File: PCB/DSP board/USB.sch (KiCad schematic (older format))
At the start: 24 parts, among them J5 USB_B, U8 USB3300-EZK, Y3 24MHz

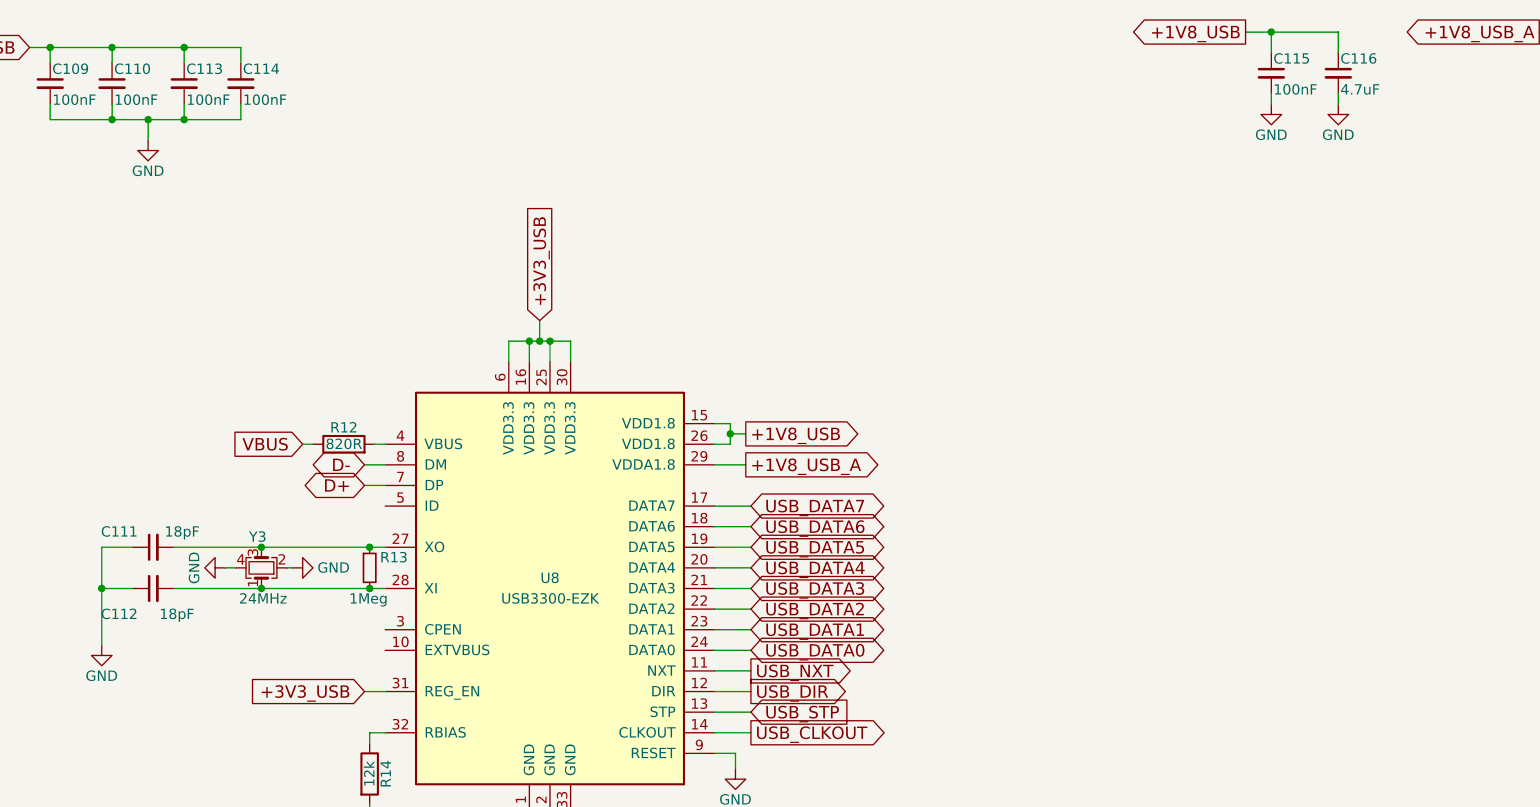
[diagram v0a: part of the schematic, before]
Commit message: Schematics + Footprints Rev.1
Ready to route.
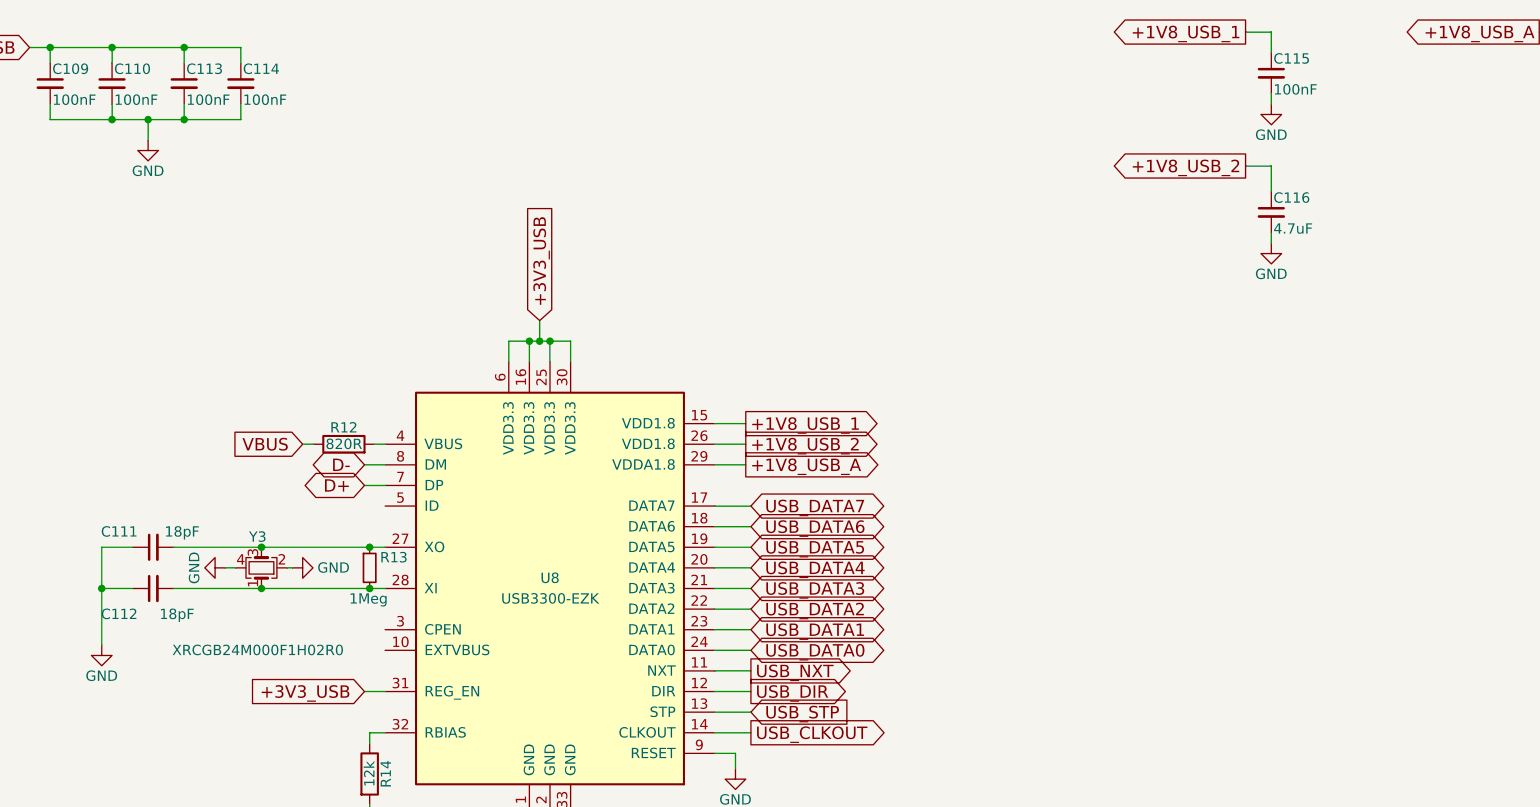
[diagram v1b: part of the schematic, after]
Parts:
- C105, C106, C109, C110, C111, C112, C113, C114, C115, C117: footprint (none) -> Capacitors_SMD:C_0603
- C107, C108, C116, C118: footprint (none) -> Capacitors_SMD:C_0805
- J5: footprint (none) -> USB_Connector:USB_B_2.0
- L12: footprint (none) -> Inductors_SMD:L_0603
- R12, R13, R14: footprint (none) -> Resistors_SMD:R_0603
- RN24, RN25, RN26: footprint (none) -> Resistor:0603_RN4
- Y3: value 24MHz -> XRCGB24M000F1H02R0; footprint (none) -> Crystals:Crystal_SMD_2016-4pin_2.0x1.6mm
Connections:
- net +1V8_USB renamed +1V8_USB_1
- net +1V8_USB_1: no longer C116.1, U8.26 (VDD1.8)
- new net +1V8_USB_2: C116.1, U8.26 (VDD1.8)
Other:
- moved on the sheet: C116

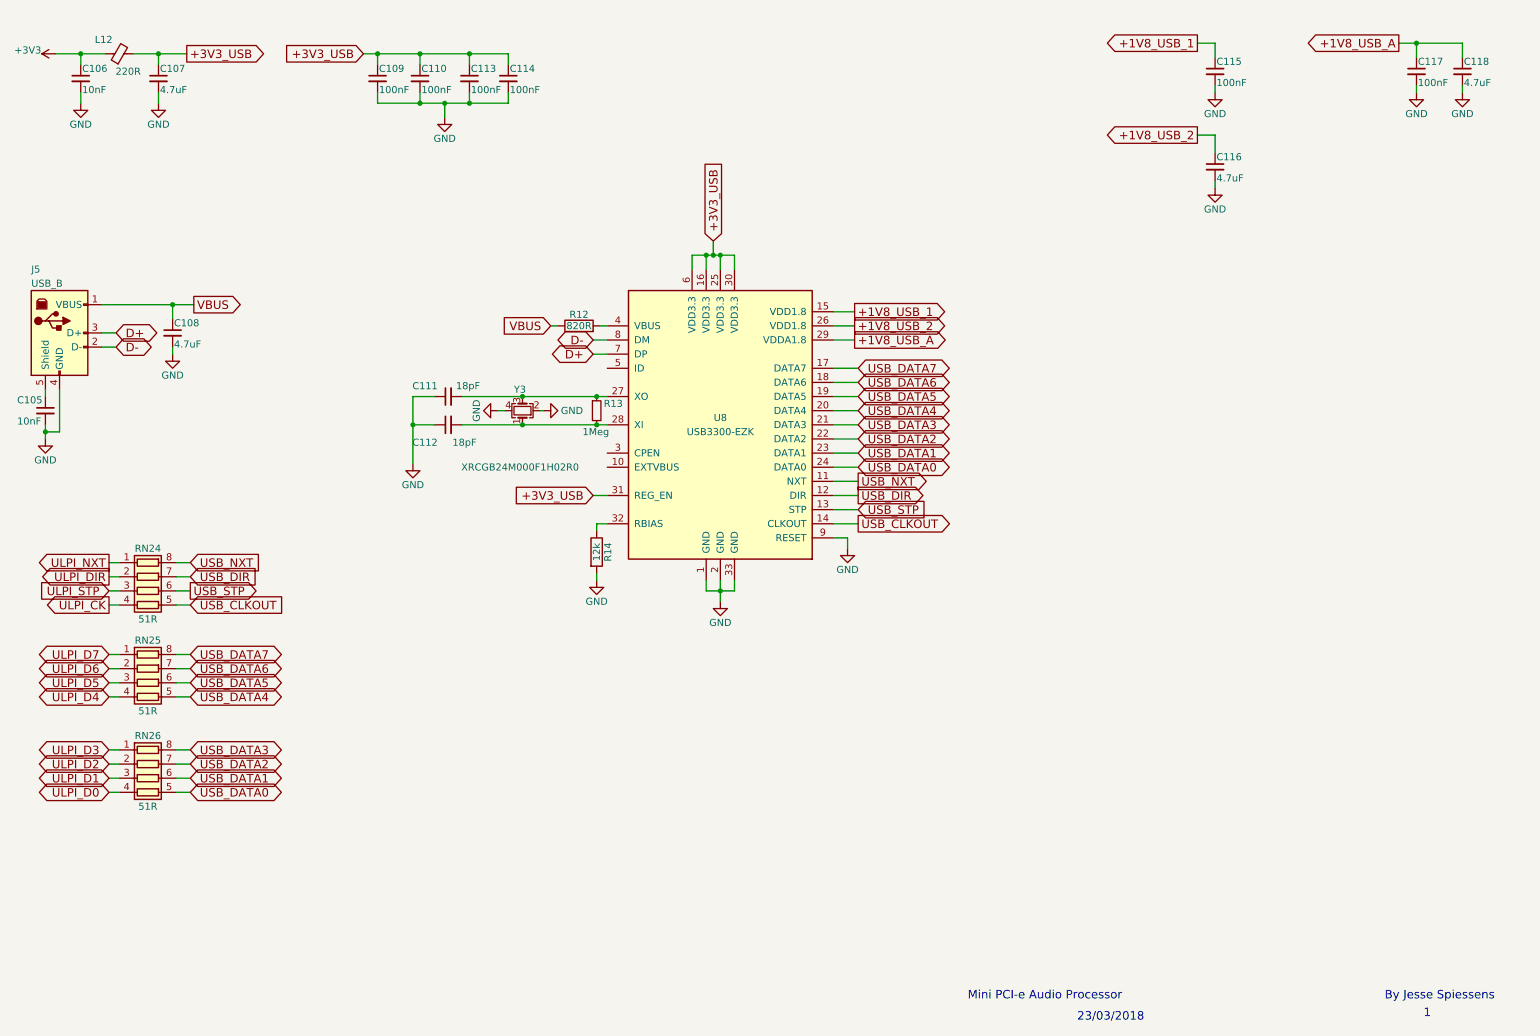
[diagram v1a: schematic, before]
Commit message: Schematics & PCB
Schematics update - ERC error fixing
PCB - setup & PCB outline
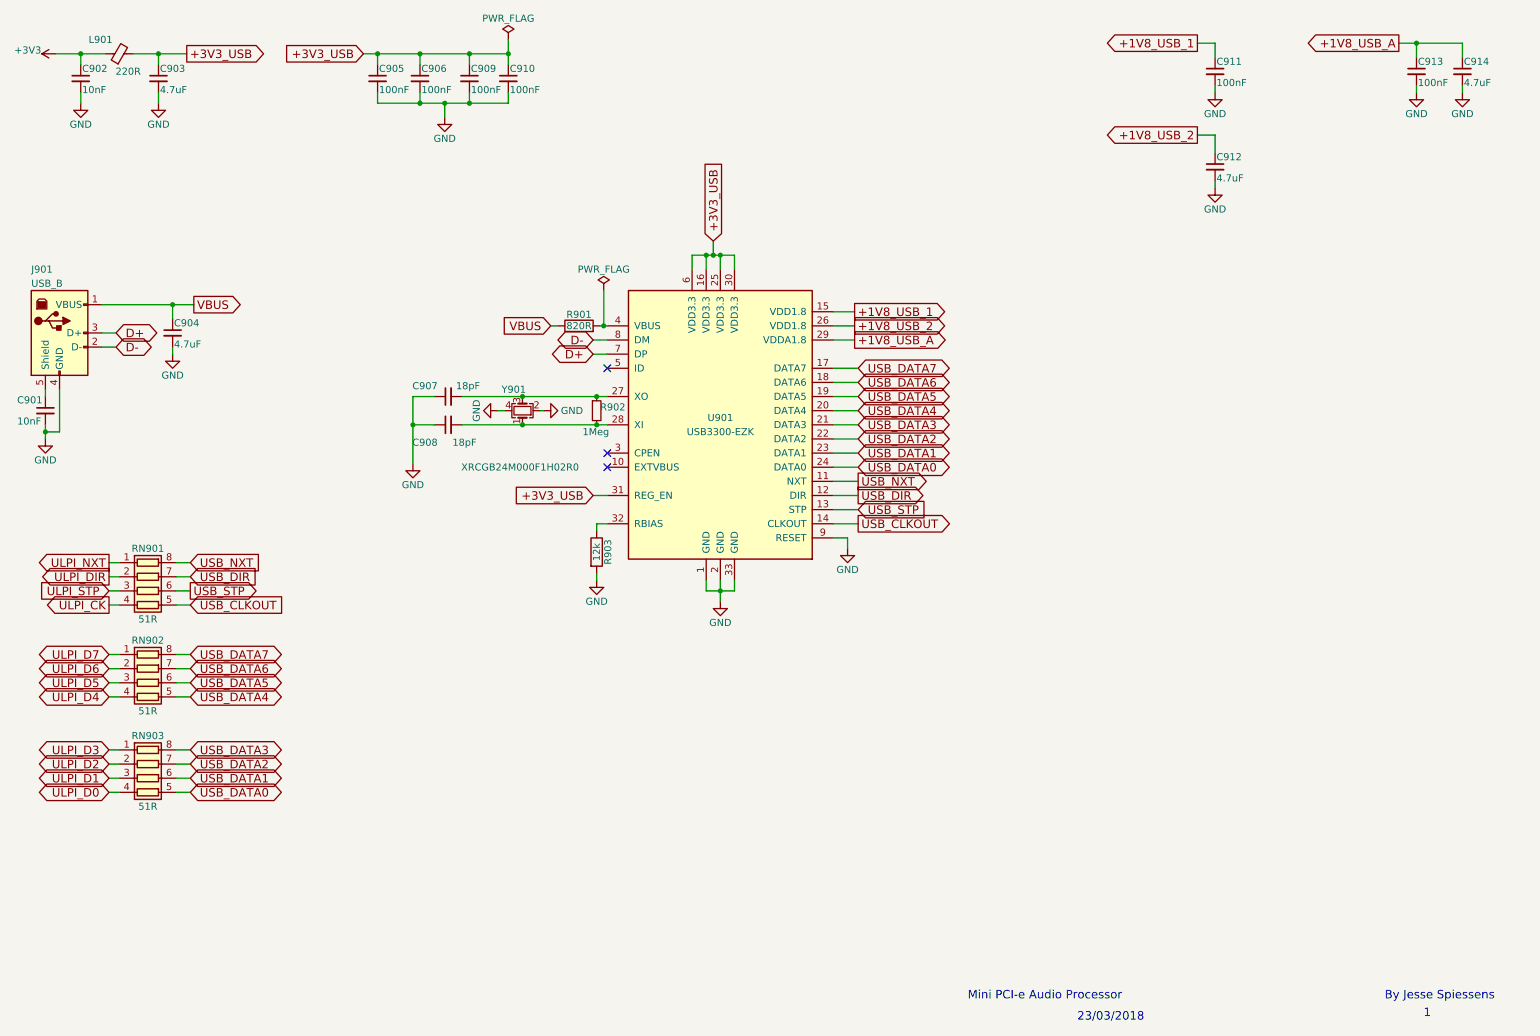
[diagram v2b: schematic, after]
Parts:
- renumbered C105 to C901, C106 to C902, C107 to C903, C108 to C904, C109 to C905, C110 to C906, C111 to C907, C112 to C908, C113 to C909, C114 to C910, C115 to C911, C116 to C912, C117 to C913, C118 to C914, J5 to J901, L12 to L901, R12 to R901, R13 to R902, R14 to R903, RN24 to RN901, RN25 to RN902, RN26 to RN903, U8 to U901, Y3 to Y901
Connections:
- no-connect marks 0 -> 3
